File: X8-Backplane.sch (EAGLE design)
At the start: 18 parts, among them U1 BD6221FSOP, U2 MIC29501-5.0WU, U3 MIC29501-5.0WU, U4 FQB27P06, U5 FQB27P06, U6 FQB27P06

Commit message: Almost done with routing - stil have to add vias and extra debugging pinouts
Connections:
- removed net BT_LED_5V: U$4G$1.15, U$4G$1.16, U6.D2
- new net +5V_BT_LED: U$4G$2.11, U$4G$2.12, U6.D2
- net +12V: now also U$4G$2.25; no longer U$4G$2.23, U$4G$2.24
- net +5V_CAMERA_TUBE: now also U$4G$2.17, U$4G$2.18, U$4G$2.19, U$4G$2.20; no longer U$4G$2.13, U$4G$2.14, U$4G$2.15, U$4G$2.16
- net +5V_LASER: now also U$4G$2.15, U$4G$2.16; no longer U$4G$2.19, U$4G$2.20
- net +5V_LED: now also U$4G$2.13, U$4G$2.14; no longer U$4G$2.17, U$4G$2.18
- net 3V3_PIEZO: now also U$4G$2.23, U$4G$2.24; no longer U$4G$1.10, U$4G$1.9
- net GND_PIEZO: now also U$4G$2.21, U$4G$2.22; no longer U$4G$1.11, U$4G$1.12
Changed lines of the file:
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@@
 </segment>
 <segment>
-<pinref part="U$4" gate="G$2" pin="23"/>
-<wire x1="236.22" y1="109.22" x2="233.68" y2="109.22" width="0.1524" layer="91"/>
-<pinref part="U$4" gate="G$2" pin="24"/>
-<wire x1="233.68" y1="109.22" x2="233.68" y2="114.3" width="0.1524" layer="91"/>
+<wire x1="233.68" y1="111.76" x2="233.68" y2="114.3" width="0.1524" layer="91"/>
 <wire x1="233.68" y1="114.3" x2="233.68" y2="116.84" width="0.1524" layer="91"/>
 <wire x1="233.68" y1="116.84" x2="233.68" y2="124.46" width="0.1524" layer="91"/>
 <wire x1="233.68" y1="124.46" x2="233.68" y2="132.08" width="0.1524" layer="91"/>
-<wire x1="251.46" y1="109.22" x2="254" y2="109.22" width="0.1524" layer="91"/>
-<wire x1="254" y1="109.22" x2="254" y2="111.76" width="0.1524" layer="91"/>
 <wire x1="254" y1="111.76" x2="254" y2="114.3" width="0.1524" layer="91"/>
 <wire x1="254" y1="114.3" x2="254" y2="116.84" width="0.1524" layer="91"/>
@@
 <pinref part="U$4" gate="G$2" pin="26"/>
 <wire x1="251.46" y1="111.76" x2="254" y2="111.76" width="0.1524" layer="91"/>
-<junction x="254" y="111.76"/>
 <pinref part="U$4" gate="G$2" pin="28"/>
 <wire x1="251.46" y1="114.3" x2="254" y2="114.3" width="0.1524" layer="91"/>
@@
 <junction x="254" y="116.84"/>
 <pinref part="P+4" gate="1" pin="+12V"/>
+<pinref part="U$4" gate="G$2" pin="25"/>
+<wire x1="233.68" y1="111.76" x2="236.22" y2="111.76" width="0.1524" layer="91"/>
 </segment>
 <segment>
@@
 </segment>
 <segment>
-<pinref part="U$4" gate="G$2" pin="13"/>
-<wire x1="233.68" y1="99.06" x2="233.68" y2="96.52" width="0.1524" layer="91"/>
-<wire x1="233.68" y1="96.52" x2="236.22" y2="96.52" width="0.1524" layer="91"/>
-<pinref part="U$4" gate="G$2" pin="15"/>
-<wire x1="236.22" y1="99.06" x2="233.68" y2="99.06" width="0.1524" layer="91"/>
-<junction x="233.68" y="99.06"/>
-<wire x1="233.68" y1="99.06" x2="223.52" y2="99.06" width="0.1524" layer="91"/>
-<label x="223.52" y="91.44" size="1.778" layer="95" rot="R90"/>
-</segment>
-<segment>
-<wire x1="254" y1="99.06" x2="254" y2="96.52" width="0.1524" layer="91"/>
-<pinref part="U$4" gate="G$2" pin="16"/>
-<wire x1="251.46" y1="99.06" x2="254" y2="99.06" width="0.1524" layer="91"/>
-<junction x="254" y="99.06"/>
-<pinref part="U$4" gate="G$2" pin="14"/>
-<wire x1="251.46" y1="96.52" x2="254" y2="96.52" width="0.1524" layer="91"/>
-<wire x1="254" y1="99.06" x2="261.62" y2="99.06" width="0.1524" layer="91"/>
-<label x="266.7" y="91.44" size="1.778" layer="95" rot="R90"/>
-</segment>
-<segment>
 <pinref part="U6" gate="G$1" pin="S2"/>
 <wire x1="535.94" y1="124.46" x2="535.94" y2="132.08" width="0.1524" layer="91"/>
 <label x="525.78" y="132.08" size="1.778" layer="95"/>
+</segment>
+<segment>
+<pinref part="U$4" gate="G$2" pin="19"/>
+<wire x1="236.22" y1="104.14" x2="233.68" y2="104.14" width="0.1524" layer="91"/>
+<wire x1="233.68" y1="104.14" x2="233.68" y2="101.6" width="0.1524" layer="91"/>
+<pinref part="U$4" gate="G$2" pin="17"/>
+<wire x1="233.68" y1="101.6" x2="236.22" y2="101.6" width="0.1524" layer="91"/>
+<wire x1="233.68" y1="101.6" x2="228.6" y2="101.6" width="0.1524" layer="91"/>
+<junction x="233.68" y="101.6"/>
+<label x="223.52" y="101.6" size="1.778" layer="95"/>
+</segment>
+<segment>
+<pinref part="U$4" gate="G$2" pin="18"/>
+<wire x1="251.46" y1="101.6" x2="254" y2="101.6" width="0.1524" layer="91"/>
+<wire x1="254" y1="101.6" x2="254" y2="104.14" width="0.1524" layer="91"/>
+<pinref part="U$4" gate="G$2" pin="20"/>
+<wire x1="254" y1="104.14" x2="251.46" y2="104.14" width="0.1524" layer="91"/>
+<wire x1="254" y1="101.6" x2="259.08" y2="101.6" width="0.1524" layer="91"/>
+<junction x="254" y="101.6"/>
+<label x="251.46" y="101.6" size="1.778" layer="95"/>
 </segment>
 </net>
@@
 </segment>
 <segment>
-<pinref part="U$4" gate="G$1" pin="10"/>
-<wire x1="182.88" y1="91.44" x2="170.18" y2="91.44" width="0.1524" layer="91"/>
-<label x="170.18" y="91.44" size="1.778" layer="95"/>
-</segment>
-<segment>
-<pinref part="U$4" gate="G$1" pin="9"/>
-<wire x1="198.12" y1="91.44" x2="205.74" y2="91.44" width="0.1524" layer="91"/>
-<label x="200.66" y="91.44" size="1.778" layer="95"/>
+<pinref part="U$4" gate="G$2" pin="23"/>
+<wire x1="236.22" y1="109.22" x2="233.68" y2="109.22" width="0.1524" layer="91"/>
+<label x="226.06" y="109.22" size="1.778" layer="95"/>
+</segment>
+<segment>
+<pinref part="U$4" gate="G$2" pin="24"/>
+<wire x1="251.46" y1="109.22" x2="254" y2="109.22" width="0.1524" layer="91"/>
+<label x="251.46" y="109.22" size="1.778" layer="95"/>
 </segment>
 </net>
@@
 </segment>
 <segment>
-<pinref part="U$4" gate="G$1" pin="12"/>
-<wire x1="182.88" y1="93.98" x2="170.18" y2="93.98" width="0.1524" layer="91"/>
-<label x="170.18" y="93.98" size="1.778" layer="95"/>
-</segment>
-<segment>
-<pinref part="U$4" gate="G$1" pin="11"/>
-<wire x1="198.12" y1="93.98" x2="205.74" y2="93.98" width="0.1524" layer="91"/>
-<label x="200.66" y="93.98" size="1.778" layer="95"/>
+<pinref part="U$4" gate="G$2" pin="21"/>
+<wire x1="236.22" y1="106.68" x2="233.68" y2="106.68" width="0.1524" layer="91"/>
+<label x="226.06" y="106.68" size="1.778" layer="95"/>
+</segment>
+<segment>
+<pinref part="U$4" gate="G$2" pin="22"/>
+<wire x1="251.46" y1="106.68" x2="254" y2="106.68" width="0.1524" layer="91"/>
+<label x="251.46" y="106.68" size="1.778" layer="95"/>
 </segment>
 </net>
@@
 </segment>
 <segment>
-<pinref part="U$4" gate="G$2" pin="18"/>
-<wire x1="251.46" y1="101.6" x2="261.62" y2="101.6" width="0.1524" layer="91"/>
-<label x="254" y="101.6" size="1.778" layer="95"/>
-</segment>
-<segment>
-<pinref part="U$4" gate="G$2" pin="17"/>
-<wire x1="236.22" y1="101.6" x2="226.06" y2="101.6" width="0.1524" layer="91"/>
-<label x="226.06" y="101.6" size="1.778" layer="95"/>
+<pinref part="U$4" gate="G$2" pin="13"/>
+<wire x1="236.22" y1="96.52" x2="228.6" y2="96.52" width="0.1524" layer="91"/>
+<label x="223.52" y="96.52" size="1.778" layer="95"/>
+</segment>
+<segment>
+<pinref part="U$4" gate="G$2" pin="14"/>
+<wire x1="251.46" y1="96.52" x2="259.08" y2="96.52" width="0.1524" layer="91"/>
+<label x="251.46" y="96.52" size="1.778" layer="95"/>
 </segment>
 </net>
@@
 </segment>
 <segment>
-<pinref part="U$4" gate="G$2" pin="20"/>
-<wire x1="251.46" y1="104.14" x2="261.62" y2="104.14" width="0.1524" layer="91"/>
-<label x="254" y="104.14" size="1.778" layer="95"/>
-</segment>
-<segment>
-<pinref part="U$4" gate="G$2" pin="19"/>
-<wire x1="236.22" y1="104.14" x2="226.06" y2="104.14" width="0.1524" layer="91"/>
-<label x="226.06" y="104.14" size="1.778" layer="95"/>
+<pinref part="U$4" gate="G$2" pin="15"/>
+<wire x1="236.22" y1="99.06" x2="228.6" y2="99.06" width="0.1524" layer="91"/>
+<label x="223.52" y="99.06" size="1.778" layer="95"/>
+</segment>
+<segment>
+<pinref part="U$4" gate="G$2" pin="16"/>
+<wire x1="251.46" y1="99.06" x2="259.08" y2="99.06" width="0.1524" layer="91"/>
+<label x="251.46" y="99.06" size="1.778" layer="95"/>
 </segment>
 </net>
@@
 </segment>
 </net>
-<net name="BT_LED_5V" class="0">
+<net name="+5V_BT_LED" class="0">
 <segment>
 <pinref part="U6" gate="G$1" pin="D2"/>
@@
 </segment>
 <segment>
-<pinref part="U$4" gate="G$1" pin="16"/>
-<wire x1="182.88" y1="99.06" x2="170.18" y2="99.06" width="0.1524" layer="91"/>
-<label x="170.18" y="99.06" size="1.778" layer="95"/>
-</segment>
-<segment>
-<pinref part="U$4" gate="G$1" pin="15"/>
-<wire x1="198.12" y1="99.06" x2="208.28" y2="99.06" width="0.1524" layer="91"/>
-<label x="200.66" y="99.06" size="1.778" layer="95"/>
-</segment>
-</net>
+<pinref part="U$4" gate="G$2" pin="11"/>
+<wire x1="236.22" y1="93.98" x2="228.6" y2="93.98" width="0.1524" layer="91"/>
+<label x="223.52" y="93.98" size="1.778" layer="95"/>
+</segment>
+<segment>
+<pinref part="U$4" gate="G$2" pin="12"/>
+<wire x1="251.46" y1="93.98" x2="259.08" y2="93.98" width="0.1524" layer="91"/>
+<label x="251.46" y="93.98" size="1.778" layer="95"/>
+</segment>
+</net>

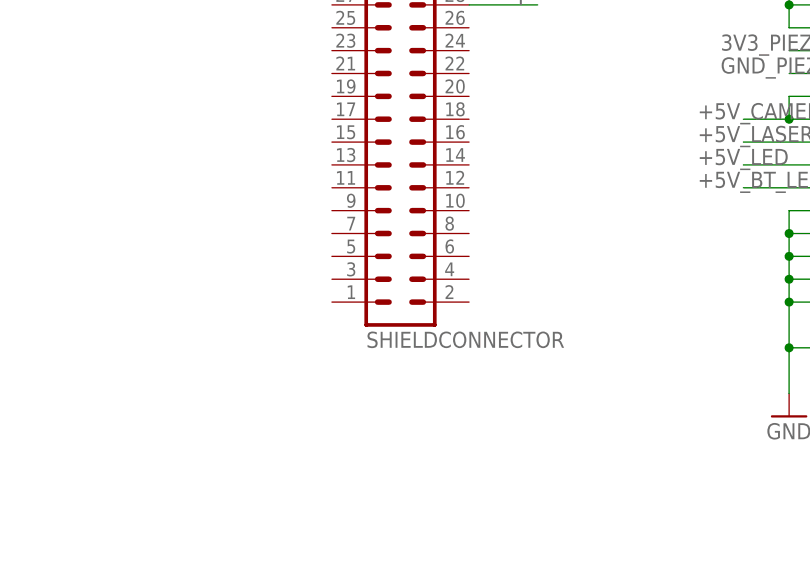
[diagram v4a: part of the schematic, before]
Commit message: Finished routing except for any debug pins and possible extra vias
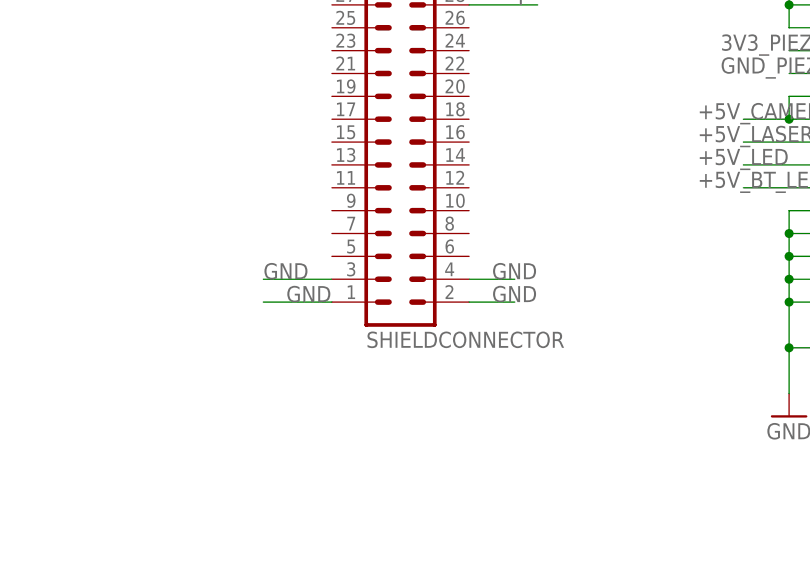
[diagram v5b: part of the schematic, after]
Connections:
- net GND: now also U$4G$1.1, U$4G$1.2, U$4G$1.3, U$4G$1.4
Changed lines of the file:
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@@
 <pinref part="GND16" gate="1" pin="GND"/>
+</segment>
+<segment>
+<pinref part="U$4" gate="G$1" pin="3"/>
+<wire x1="198.12" y1="83.82" x2="203.2" y2="83.82" width="0.1524" layer="91"/>
+<label x="200.66" y="83.82" size="1.778" layer="95"/>
+</segment>
+<segment>
+<pinref part="U$4" gate="G$1" pin="1"/>
+<wire x1="198.12" y1="81.28" x2="203.2" y2="81.28" width="0.1524" layer="91"/>
+<label x="200.66" y="81.28" size="1.778" layer="95"/>
+</segment>
+<segment>
+<pinref part="U$4" gate="G$1" pin="2"/>
+<wire x1="182.88" y1="81.28" x2="175.26" y2="81.28" width="0.1524" layer="91"/>
+<label x="177.8" y="81.28" size="1.778" layer="95"/>
+</segment>
+<segment>
+<pinref part="U$4" gate="G$1" pin="4"/>
+<wire x1="182.88" y1="83.82" x2="175.26" y2="83.82" width="0.1524" layer="91"/>
+<label x="175.26" y="83.82" size="1.778" layer="95"/>
 </segment>
 </net>

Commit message: minor changes by Ryan
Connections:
- net A renamed TX_H
- net B renamed TX_L
- net Y renamed RX_L
- net Z renamed RX_H
- net 3.3V: now also U$4G$1.25, U$4G$1.26

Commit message: added buck regulator
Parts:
- removed C1, C7: 10uF, SparkFun-Passives:CAP0603-CAP
- removed C5, C8: 0.1uF, SparkFun-Passives:CAP0603-CAP
- removed R1, R2: 10k, SparkFun-Passives:RESISTOR0603-RES
- removed U2, U3: MIC29501-5.0WU, LDO:MIC29501-5.0WU
- added C10, C6, C9: 150uF, PowerComponents:C-TANTALUM(10UF_150UF)
- added C11, C12, C13, C2: 10uF, PowerComponents:C-TANTALUM(10UF_150UF)
- added C3: 0.47uF, SparkFun-Capacitors:CAP0805
- added C4: 0.01uF, SparkFun-Passives:CAP0603-CAP
- added U$2: SWITCHMODE_SCHOTTKY, PowerComponents:SWITCHMODE_SCHOTTKY
- added U$6: 15uH, DiscreteComponents:HCMA1305
- added U7: LM2678, PowerComponents:LM2678
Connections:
- removed net +5V_CAMERA_TUBE: C7.1, U$4G$2.17, U$4G$2.18, U$4G$2.19, U$4G$2.20, U3.OUT, U4.S2, U5.S2, U6.S2
- removed net EN1: R1.1, U2.EN
- removed net EN2: R2.1, U3.EN
- new net N$18: C4.1, U7.BOOST
- new net N$19: C4.2, U$2.P$4, U$6.1, U7.OUTPUT
- net +12V: now also C11.+, C12.+, C13.+, C2.+, C3.1, U7.VIN; no longer C5.1, C8.1, R1.2, R2.2, U2.IN, U3.IN
- net +5V: now also C10.+, C6.+, C9.+, U$4G$2.17, U$4G$2.18, U$4G$2.19, U$4G$2.20, U$6.2, U4.S2, U5.S2, U6.S2, U7.FEEDBACK; no longer C1.1, U2.OUT
- net GND: now also C10.-, C11.-, C12.-, C13.-, C2.-, C3.2, C6.-, C9.-, U$2.P$1, U$2.P$3, U7.GND, U7.TABGND; no longer C1.2, C5.2, C7.2, C8.2, U2.6, U2.GND, U3.6, U3.GND
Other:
- note removed: "Linear regulator for camera"

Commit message: added LEDs
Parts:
- added LED1, LED2, LED3, LED4, LED5: (no value), led:LEDSML0603
- added R1, R3, R4, R5: 330, resistor:R-US_R0603
- added R2: 1k, resistor:R-US_R0603
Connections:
- new net N$2: LED5.A, R1.1
- new net N$3: LED4.A, R2.1
- new net N$4: LED1.A, R5.1
- new net N$5: LED2.A, R4.1
- new net N$6: LED3.A, R3.1
- net +12V: now also R2.2
- net +5V: now also R1.2
- net +5V_BT_LED: now also R3.2
- net +5V_LASER: now also R4.2
- net +5V_LED: now also R5.2
- net GND: now also LED1.C, LED2.C, LED3.C, LED4.C, LED5.C
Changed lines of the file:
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@@
 <part name="RPI+5V4" library="supply1" deviceset="+5V" device="" value="+5V"/>
 <part name="RPI+5V5" library="supply1" deviceset="+5V" device="" value="+5V"/>
+<part name="LED5" library="led" deviceset="LED" device="SML0603"/>
+<part name="R1" library="resistor" deviceset="R-US_" device="R0603" value="330"/>
+<part name="R2" library="resistor" deviceset="R-US_" device="R0603" value="1k"/>
+<part name="R3" library="resistor" deviceset="R-US_" device="R0603" value="330"/>
+<part name="R4" library="resistor" deviceset="R-US_" device="R0603" value="330"/>
+<part name="R5" library="resistor" deviceset="R-US_" device="R0603" value="330"/>
+<part name="LED1" library="led" deviceset="LED" device="SML0603"/>
+<part name="LED2" library="led" deviceset="LED" device="SML0603"/>
+<part name="LED3" library="led" deviceset="LED" device="SML0603"/>
+<part name="GND3" library="SparkFun-Aesthetics" deviceset="GND" device=""/>
+<part name="GND4" library="SparkFun-Aesthetics" deviceset="GND" device=""/>
+<part name="GND7" library="SparkFun-Aesthetics" deviceset="GND" device=""/>
+<part name="GND18" library="SparkFun-Aesthetics" deviceset="GND" device=""/>
+<part name="P+1" library="supply1" deviceset="+5V" device=""/>
+<part name="LED4" library="led" deviceset="LED" device="SML0603"/>
+<part name="GND19" library="SparkFun-Aesthetics" deviceset="GND" device=""/>
+<part name="P+3" library="supply1" deviceset="+12V" device=""/>
 </parts>
 <sheets>
@@
 <attribute name="VALUE" x="226.06" y="101.6" size="1.778" layer="96" rot="MR0"/>
 </instance>
+<instance part="LED5" gate="G$1" x="205.74" y="-152.4"/>
+<instance part="R1" gate="G$1" x="205.74" y="-139.7" rot="R90"/>
+<instance part="R2" gate="G$1" x="17.78" y="-124.46" rot="R90"/>
+<instance part="R3" gate="G$1" x="543.56" y="96.52" rot="R90"/>
+<instance part="R4" gate="G$1" x="548.64" y="149.86" rot="R90"/>
+<instance part="R5" gate="G$1" x="495.3" y="149.86" rot="R90"/>
+<instance part="LED1" gate="G$1" x="495.3" y="139.7"/>
+<instance part="LED2" gate="G$1" x="548.64" y="139.7"/>
+<instance part="LED3" gate="G$1" x="543.56" y="86.36"/>
+<instance part="GND3" gate="1" x="495.3" y="127"/>
+<instance part="GND4" gate="1" x="548.64" y="129.54"/>
+<instance part="GND7" gate="1" x="543.56" y="76.2"/>
+<instance part="GND18" gate="1" x="205.74" y="-165.1"/>
+<instance part="P+1" gate="1" x="205.74" y="-127" smashed="yes">
+<attribute name="VALUE" x="208.28" y="-129.54" size="1.778" layer="96"/>
+</instance>
+<instance part="LED4" gate="G$1" x="17.78" y="-139.7"/>
+<instance part="GND19" gate="1" x="17.78" y="-152.4"/>
+<instance part="P+3" gate="1" x="17.78" y="-111.76"/>
 </instances>
 <busses>
@@
 <pinref part="GND2" gate="1" pin="GND"/>
 </segment>
+<segment>
+<pinref part="LED1" gate="G$1" pin="C"/>
+<pinref part="GND3" gate="1" pin="GND"/>
+<wire x1="495.3" y1="129.54" x2="495.3" y2="134.62" width="0.1524" layer="91"/>
+</segment>
+<segment>
+<pinref part="GND4" gate="1" pin="GND"/>
+<pinref part="LED2" gate="G$1" pin="C"/>
+<wire x1="548.64" y1="132.08" x2="548.64" y2="134.62" width="0.1524" layer="91"/>
+</segment>
+<segment>
+<pinref part="GND7" gate="1" pin="GND"/>
+<pinref part="LED3" gate="G$1" pin="C"/>
+<wire x1="543.56" y1="81.28" x2="543.56" y2="78.74" width="0.1524" layer="91"/>
+</segment>
+<segment>
+<pinref part="GND18" gate="1" pin="GND"/>
+<pinref part="LED5" gate="G$1" pin="C"/>
+<wire x1="205.74" y1="-157.48" x2="205.74" y2="-162.56" width="0.1524" layer="91"/>
+</segment>
+<segment>
+<pinref part="LED4" gate="G$1" pin="C"/>
+<pinref part="GND19" gate="1" pin="GND"/>
+<wire x1="17.78" y1="-144.78" x2="17.78" y2="-149.86" width="0.1524" layer="91"/>
+</segment>
 </net>
 <net name="+12V" class="0">
@@
 <junction x="58.42" y="-139.7"/>
 </segment>
+<segment>
+<pinref part="P+3" gate="1" pin="+12V"/>
+<pinref part="R2" gate="G$1" pin="2"/>
+<wire x1="17.78" y1="-114.3" x2="17.78" y2="-119.38" width="0.1524" layer="91"/>
+</segment>
 </net>
 <net name="+5V" class="0">
@@
 <pinref part="RPI+5V5" gate="1" pin="+5V"/>
 </segment>
+<segment>
+<pinref part="P+1" gate="1" pin="+5V"/>
+<pinref part="R1" gate="G$1" pin="2"/>
+<wire x1="205.74" y1="-129.54" x2="205.74" y2="-134.62" width="0.1524" layer="91"/>
+</segment>
 </net>
 <net name="3.3V" class="0">
@@
 <segment>
 <pinref part="U4" gate="G$1" pin="D2"/>
-<wire x1="487.68" y1="160.02" x2="487.68" y2="149.86" width="0.1524" layer="91"/>
+<wire x1="487.68" y1="160.02" x2="487.68" y2="157.48" width="0.1524" layer="91"/>
 <label x="485.14" y="147.32" size="1.778" layer="95"/>
+<pinref part="R5" gate="G$1" pin="2"/>
+<wire x1="487.68" y1="157.48" x2="487.68" y2="149.86" width="0.1524" layer="91"/>
+<wire x1="495.3" y1="154.94" x2="495.3" y2="157.48" width="0.1524" layer="91"/>
+<wire x1="495.3" y1="157.48" x2="487.68" y2="157.48" width="0.1524" layer="91"/>
+<junction x="487.68" y="157.48"/>
 </segment>
 <segment>
@@
 <segment>
 <pinref part="U5" gate="G$1" pin="D2"/>
-<wire x1="538.48" y1="160.02" x2="538.48" y2="152.4" width="0.1524" layer="91"/>
+<wire x1="538.48" y1="160.02" x2="538.48" y2="157.48" width="0.1524" layer="91"/>
 <label x="533.4" y="149.86" size="1.778" layer="95"/>
+<pinref part="R4" gate="G$1" pin="2"/>
+<wire x1="538.48" y1="157.48" x2="538.48" y2="152.4" width="0.1524" layer="91"/>
+<wire x1="548.64" y1="154.94" x2="548.64" y2="157.48" width="0.1524" layer="91"/>
+<wire x1="548.64" y1="157.48" x2="538.48" y2="157.48" width="0.1524" layer="91"/>
+<junction x="538.48" y="157.48"/>
 </segment>
 <segment>
@@
 <segment>
 <pinref part="U6" gate="G$1" pin="D2"/>
-<wire x1="535.94" y1="106.68" x2="535.94" y2="99.06" width="0.1524" layer="91"/>
+<wire x1="535.94" y1="106.68" x2="535.94" y2="104.14" width="0.1524" layer="91"/>
 <label x="530.86" y="96.52" size="1.778" layer="95"/>
+<pinref part="R3" gate="G$1" pin="2"/>
+<wire x1="535.94" y1="104.14" x2="535.94" y2="99.06" width="0.1524" layer="91"/>
+<wire x1="543.56" y1="101.6" x2="543.56" y2="104.14" width="0.1524" layer="91"/>
+<wire x1="543.56" y1="104.14" x2="535.94" y2="104.14" width="0.1524" layer="91"/>
+<junction x="535.94" y="104.14"/>
 </segment>
 <segment>
@@
 </segment>
 </net>
+<net name="N$4" class="0">
+<segment>
+<pinref part="R5" gate="G$1" pin="1"/>
+<pinref part="LED1" gate="G$1" pin="A"/>
+<wire x1="495.3" y1="142.24" x2="495.3" y2="144.78" width="0.1524" layer="91"/>
+</segment>
+</net>
+<net name="N$5" class="0">
+<segment>
+<pinref part="LED2" gate="G$1" pin="A"/>
+<pinref part="R4" gate="G$1" pin="1"/>
+<wire x1="548.64" y1="142.24" x2="548.64" y2="144.78" width="0.1524" layer="91"/>
+</segment>
+</net>
+<net name="N$6" class="0">
+<segment>
+<pinref part="LED3" gate="G$1" pin="A"/>
+<pinref part="R3" gate="G$1" pin="1"/>
+<wire x1="543.56" y1="88.9" x2="543.56" y2="91.44" width="0.1524" layer="91"/>
+</segment>
+</net>
+<net name="N$2" class="0">
+<segment>
+<pinref part="R1" gate="G$1" pin="1"/>
+<pinref part="LED5" gate="G$1" pin="A"/>
+<wire x1="205.74" y1="-144.78" x2="205.74" y2="-149.86" width="0.1524" layer="91"/>
+</segment>
+</net>
+<net name="N$3" class="0">
+<segment>
+<pinref part="R2" gate="G$1" pin="1"/>
+<pinref part="LED4" gate="G$1" pin="A"/>
+<wire x1="17.78" y1="-129.54" x2="17.78" y2="-137.16" width="0.1524" layer="91"/>
+</segment>
+</net>
